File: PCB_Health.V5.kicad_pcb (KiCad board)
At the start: 4 copper layers, 144.8 x 83.8 mm, 62 parts, among them J1 Conn_01x03_Socket, J2 Conn_01x02_Socket, J3 Conn_01x02_Socket, J4 Conn_01x02_Socket, J5 Conn_01x04_Socket, J6 Conn_01x04_Socket, K1 RT424012, Q1 BC337, U1 LM317_TO-220, U2 H11L1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

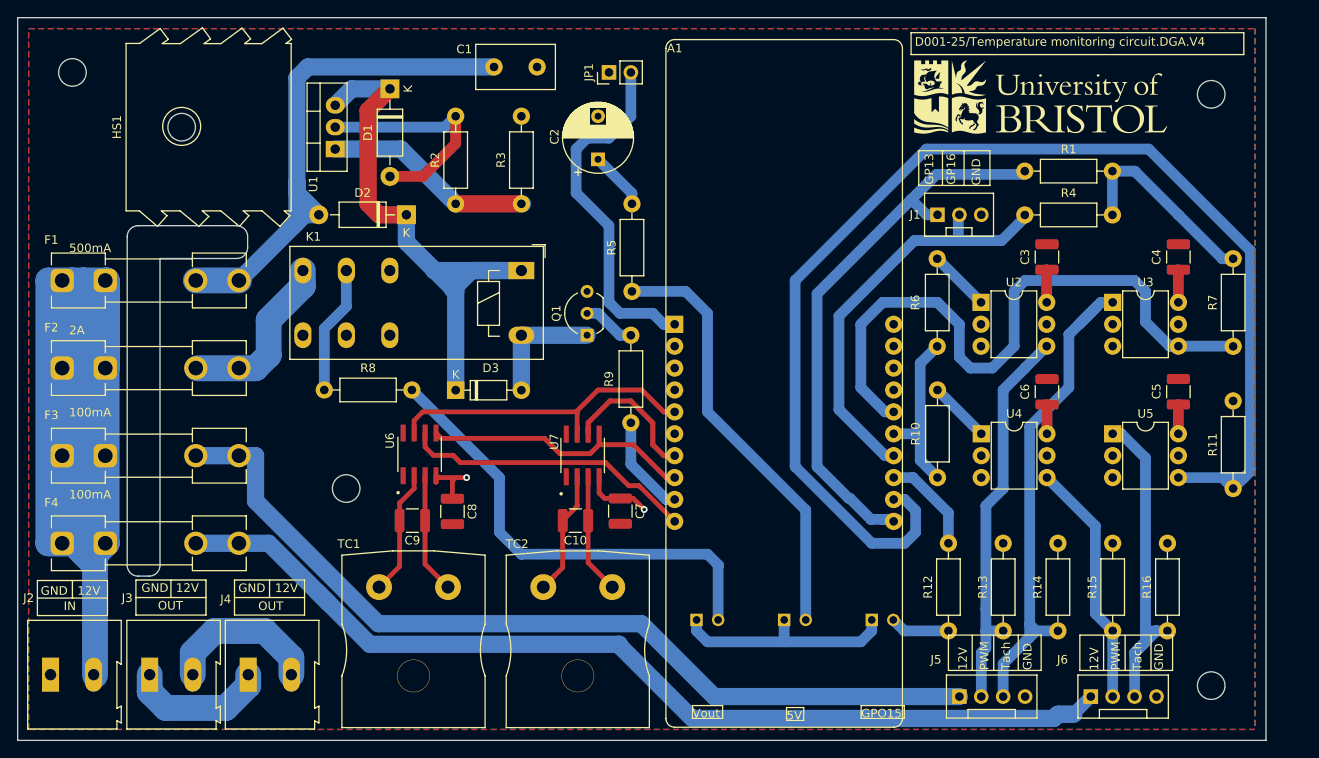
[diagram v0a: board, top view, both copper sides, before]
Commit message: Fiddled with silk screen - changed v4 to v5
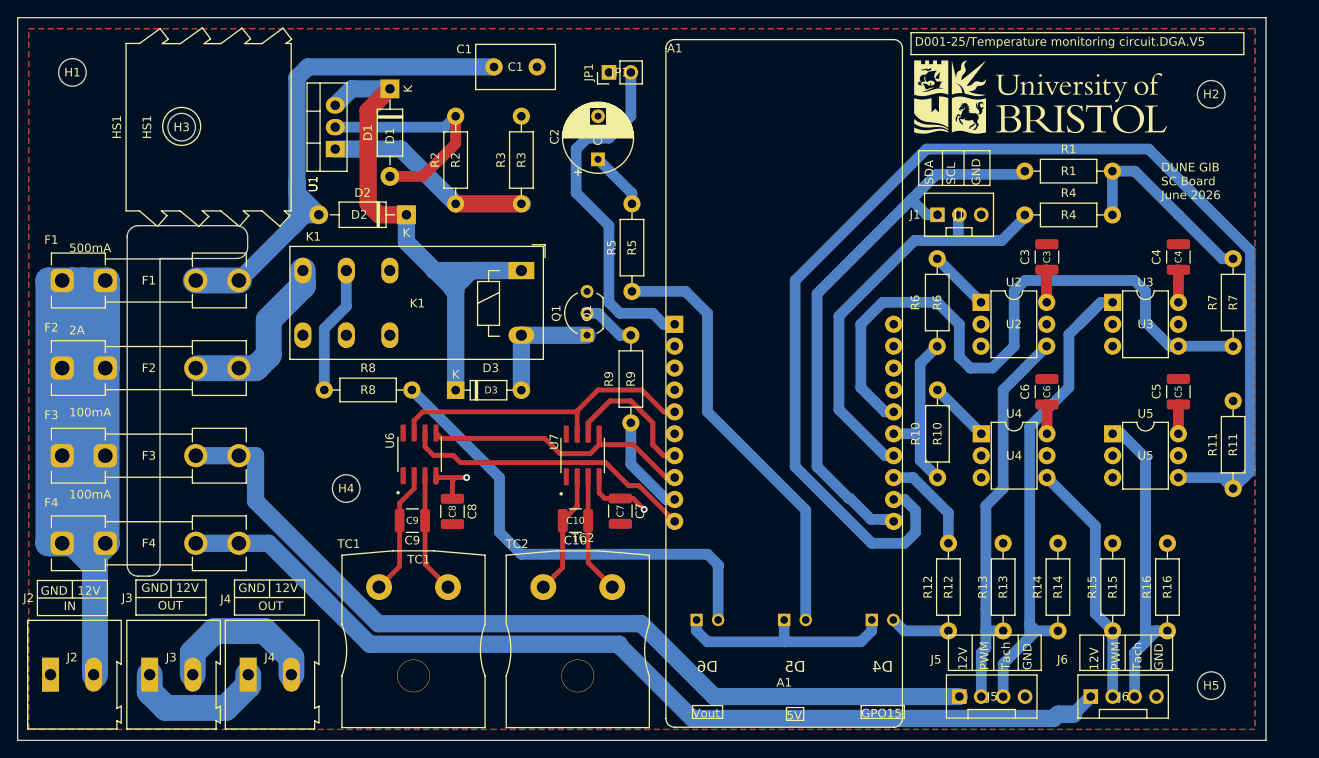
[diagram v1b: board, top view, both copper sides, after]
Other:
- board text added: "D001-25/Temperature monitoring circuit.DGA.V5"
- board text added: "DUNE GIB SC Board June 2026"
- board text added: "SCL"
- board text added: "SDA"
- board text removed: "D001-25/Temperature monitoring circuit.DGA.V4"
- board text removed: "GP13"
- board text removed: "GP16"
